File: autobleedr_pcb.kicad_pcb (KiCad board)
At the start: 2 copper layers, 4 parts, among them U1 ESP-32, U2 TMC2209, U3 Buck Converter, U4 DRV8874

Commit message: added header pins
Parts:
- added J1: Barrel_Jack, Connector_BarrelJack:BarrelJack_CUI_PJ-063AH_Horizontal, F.Cu at (149.0, 79.5)
- added J2: Conn_01x13_Pin, Connector_PinHeader_2.54mm:PinHeader_1x13_P2.54mm_Vertical, F.Cu at (99.0, 89.7)
- added J3: Conn_01x14_Pin, Connector_PinHeader_2.54mm:PinHeader_1x14_P2.54mm_Vertical, F.Cu at (134.5, 90.1)
- added J4: Conn_01x08_Socket, Connector_PinHeader_2.54mm:PinHeader_1x08_P2.54mm_Vertical, F.Cu at (186.5, 102.4)
- added J5: Conn_01x05_Pin, Connector_PinHeader_2.54mm:PinHeader_1x05_P2.54mm_Vertical, F.Cu at (167.5, 96.9)
- added J6: Conn_01x05_Pin, Connector_PinHeader_2.54mm:PinHeader_1x05_P2.54mm_Vertical, F.Cu at (142.5, 91.4)
- U1: value ESP-32 -> ~
- U2: value TMC2209 -> ~
- U3: value Buck Converter -> ~
- U4: value DRV8874 -> ~
- moved U2 103.8 mm to (193.5, 106.9), turned to -90 degrees
- moved U4 39.4 mm to (148.8, 91.8)
- moved U1 31.6 mm to (104.5, 90.4)
- moved U3 25.3 mm to (133.0, 80.5), turned to 180 degrees
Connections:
- U1 pad 1: unconnected-(U1-EN-Pad1) -> Net-(J2-Pin_1)
- U1 pad 10: unconnected-(U1-D27-Pad10) -> Net-(J2-Pin_10)
- U1 pad 11: unconnected-(U1-D14-Pad11) -> Net-(J2-Pin_11)
- U1 pad 12: unconnected-(U1-D12-Pad12) -> Net-(J2-Pin_12)
- U1 pad 13: unconnected-(U1-D13-Pad13) -> Net-(J2-Pin_13)
- U1 pad 16: unconnected-(U1-3V3-Pad16) -> Net-(J3-Pin_14)
- U1 pad 18: unconnected-(U1-D15-Pad18) -> Net-(J3-Pin_13)
- U1 pad 19: unconnected-(U1-D2-Pad19) -> Net-(J3-Pin_12)
- U1 pad 2: unconnected-(U1-VP-Pad2) -> Net-(J2-Pin_2)
- U1 pad 20: unconnected-(U1-D4-Pad20) -> Net-(J3-Pin_11)
- U1 pad 21: unconnected-(U1-RX2-Pad21) -> Net-(J3-Pin_10)
- U1 pad 22: unconnected-(U1-TX2-Pad22) -> Net-(J3-Pin_9)
- U1 pad 23: unconnected-(U1-D5-Pad23) -> Net-(J3-Pin_8)
- U1 pad 24: unconnected-(U1-D18-Pad24) -> Net-(J3-Pin_7)
- U1 pad 25: unconnected-(U1-D19-Pad25) -> Net-(J3-Pin_6)
- U1 pad 26: unconnected-(U1-D21-Pad26) -> Net-(J3-Pin_5)
- U1 pad 27: unconnected-(U1-RX0-Pad27) -> Net-(J3-Pin_4)
- U1 pad 28: unconnected-(U1-TX0-Pad28) -> Net-(J3-Pin_3)
- U1 pad 29: unconnected-(U1-D22-Pad29) -> Net-(J3-Pin_2)
- U1 pad 3: unconnected-(U1-VN-Pad3) -> Net-(J2-Pin_3)
- U1 pad 30: unconnected-(U1-D23-Pad30) -> Net-(J3-Pin_1)
- U1 pad 4: unconnected-(U1-D34-Pad4) -> Net-(J2-Pin_4)
- U1 pad 5: unconnected-(U1-D35-Pad5) -> Net-(J2-Pin_5)
- U1 pad 6: unconnected-(U1-D32-Pad6) -> Net-(J2-Pin_6)
- U1 pad 7: unconnected-(U1-D33-Pad7) -> Net-(J2-Pin_7)
- U1 pad 8: unconnected-(U1-D25-Pad8) -> Net-(J2-Pin_8)
- U1 pad 9: unconnected-(U1-D26-Pad9) -> Net-(J2-Pin_9)
- U2 pad 10: unconnected-(U2-EN-Pad10) -> Net-(J4-Pin_8)
- U2 pad 3: unconnected-(U2-DIR-Pad3) -> Net-(J4-Pin_1)
- U2 pad 4: unconnected-(U2-STEP-Pad4) -> Net-(J4-Pin_2)
- U2 pad 5: unconnected-(U2-MS1-Pad5) -> Net-(J4-Pin_3)
- U2 pad 6: unconnected-(U2-MS2-Pad6) -> Net-(J4-Pin_4)
- U2 pad 7: unconnected-(U2-DIAG-Pad7) -> Net-(J4-Pin_5)
- U2 pad 8: unconnected-(U2-INDEX-Pad8) -> Net-(J4-Pin_6)
- U2 pad 9: unconnected-(U2-UART-Pad9) -> Net-(J4-Pin_7)
- U4 pad 1: unconnected-(U4-VM-Pad1) -> Net-(J6-Pin_1)
- U4 pad 10: unconnected-(U4-IMODE-Pad10) -> Net-(J5-Pin_3)
- U4 pad 11: unconnected-(U4-OUT2-Pad11) -> Net-(J5-Pin_2)
- U4 pad 12: unconnected-(U4-OUT1-Pad12) -> Net-(J5-Pin_1)
- U4 pad 3: unconnected-(U4-EN/IN1-Pad3) -> Net-(J6-Pin_2)
- U4 pad 4: unconnected-(U4-PH/IN2-Pad4) -> Net-(J6-Pin_3)
- U4 pad 5: unconnected-(U4-PMODE-Pad5) -> Net-(J6-Pin_4)
- U4 pad 7: unconnected-(U4-VREF-Pad7) -> Net-(J6-Pin_5)
- U4 pad 8: unconnected-(U4-CS-Pad8) -> Net-(J5-Pin_5)
- U4 pad 9: unconnected-(U4-FAULT-Pad9) -> Net-(J5-Pin_4)
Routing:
- added copper zone on B.Cu, net GND

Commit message: finished initial PCB
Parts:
- added J7: Screw_Terminal_01x02, TerminalBlock:TerminalBlock_MaiXu_MX126-5.0-02P_1x02_P5.00mm, F.Cu at (149.0, 91.0)
- added J8: Conn_01x02_Pin, Connector_PinHeader_2.54mm:PinHeader_1x02_P2.54mm_Vertical, F.Cu at (139.5, 89.0)
- added J9: Conn_01x02_Pin, Connector_PinHeader_2.54mm:PinHeader_1x02_P2.54mm_Vertical, F.Cu at (139.5, 84.5)
- U1: value ~ -> ESP32
- U2: value ~ -> TMC2209
- U3: value ~ -> Buck Converter
- U4: value ~ -> DRV8874
- moved J6 69.4 mm to (75.2, 74.3)
- moved U4 68.9 mm to (83.5, 69.8)
- moved J5 68.2 mm to (103.0, 74.8)
- moved Dir 50.6 mm to (136.7, 111.7)
- moved J3 50.2 mm to (119.3, 138.0), turned to -90 degrees
- moved U2 48.8 mm to (145.7, 117.0)
- moved J2 20.7 mm to (119.1, 94.5), turned to -90 degrees
- moved U1 19.3 mm to (119.0, 103.0), turned to -90 degrees
- renumbered J4 to Dir
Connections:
- J2 pad 2: Net-(J2-Pin_2) -> unconnected-(J2-Pin_2-Pad2)
- J2 pad 3: Net-(J2-Pin_3) -> unconnected-(J2-Pin_3-Pad3)
- J6 pad 1: Net-(J6-Pin_1) -> unconnected-(J6-Pin_1-Pad1)
- J6 pad 5: Net-(J6-Pin_5) -> unconnected-(J6-Pin_5-Pad5)
- U1 pad 2: Net-(J2-Pin_2) -> unconnected-(J2-Pin_2-Pad2)
- U1 pad 3: Net-(J2-Pin_3) -> unconnected-(J2-Pin_3-Pad3)
- U4 pad 1: Net-(J6-Pin_1) -> unconnected-(J6-Pin_1-Pad1)
- U4 pad 7: Net-(J6-Pin_5) -> unconnected-(J6-Pin_5-Pad5)
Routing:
- net +3.3V: track 0.00 -> 131.3 mm
- net +12V: track 0.00 -> 70.8 mm
- net Net-(J3-Pin_14): track 0.00 -> 10.8 mm
- net unconnected-(J6-Pin_1-Pad1): track 0.00 -> 10.2 mm
- net Net-(J3-Pin_9): track 0.00 -> 9.71 mm
- net Net-(J3-Pin_7): track 0.00 -> 9.71 mm
- net Net-(J3-Pin_5): track 0.00 -> 9.71 mm
- net Net-(J3-Pin_4): track 0.00 -> 9.71 mm
- net Net-(J3-Pin_3): track 0.00 -> 9.71 mm
- net Net-(J3-Pin_2): track 0.00 -> 9.71 mm
- net Net-(J3-Pin_12): track 0.00 -> 9.71 mm
- net Net-(J3-Pin_11): track 0.00 -> 9.71 mm
- net Net-(J3-Pin_8): track 0.00 -> 9.71 mm
- net Net-(J3-Pin_6): track 0.00 -> 9.71 mm
- net Net-(J3-Pin_13): track 0.00 -> 9.71 mm
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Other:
- board outline added: 91 x 78.5 mm
- board text added: "12V"
- board text added: "3.3V"
- board text added: "AutoBleedr"
- board text added: "Vin"

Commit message: resubmit update 1
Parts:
- added J10: XT60 Connector, Connector_AMASS:AMASS_XT60PW-F_1x02_P7.20mm_Horizontal, F.Cu at (141.8, 93.1)
- U1: value ESP32 -> ~
- U2: value TMC2209 -> ~
- U3: value Buck Converter -> ~
- U4: value DRV8874 -> ~
- moved J4 14.5 mm to (124.0, 118.5)
- moved U2 14.5 mm to (133.0, 123.9)
- moved J7 14.1 mm to (145.0, 104.5)
- moved J8 10.8 mm to (128.7, 90.0)
- moved J9 10.8 mm to (128.7, 85.5)
- moved J1 8.06 mm to (145.0, 72.5), turned to 90 degrees
- moved U1 7.46 mm to (111.6, 102.9)
- moved J2 7.46 mm to (111.7, 94.4)
- moved J3 7.46 mm to (111.8, 137.9)
- renumbered Dir to J4
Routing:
- net +3.3V: track 131.3 -> 48.6 mm
- net +12V: track 70.8 -> 38.7 mm
- net Net-(J4-Pin_4): track 9.10 -> 18.2 mm
- net Net-(J4-Pin_8): track 9.10 -> 0.00 mm
- net Net-(J4-Pin_7): track 9.10 -> 0.00 mm
- net Net-(J4-Pin_5): track 9.10 -> 18.2 mm
- net Net-(J4-Pin_6): track 9.10 -> 0.00 mm
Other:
- board text added: "AutoBleedr Version 1"
- board text removed: "AutoBleedr"

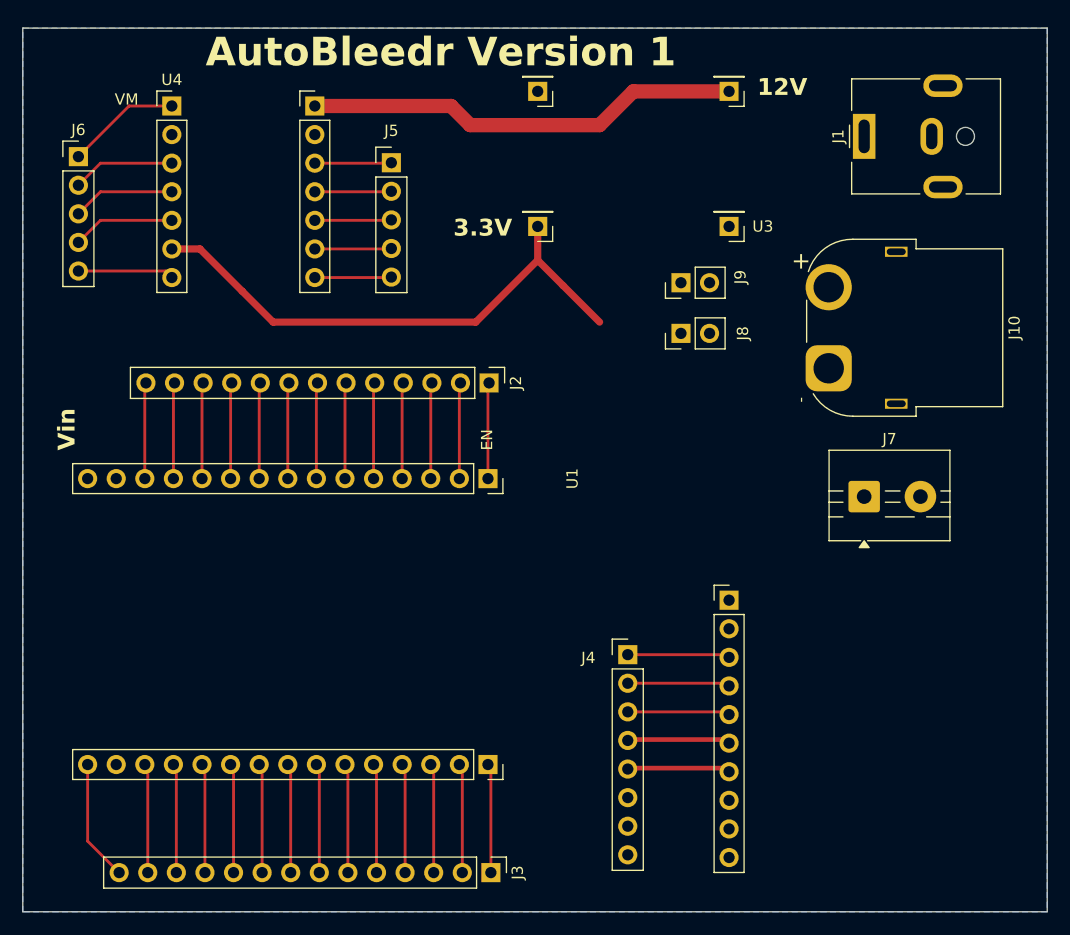
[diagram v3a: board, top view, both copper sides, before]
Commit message: Updated buck converter footprint, added stitching vias, test points, traces
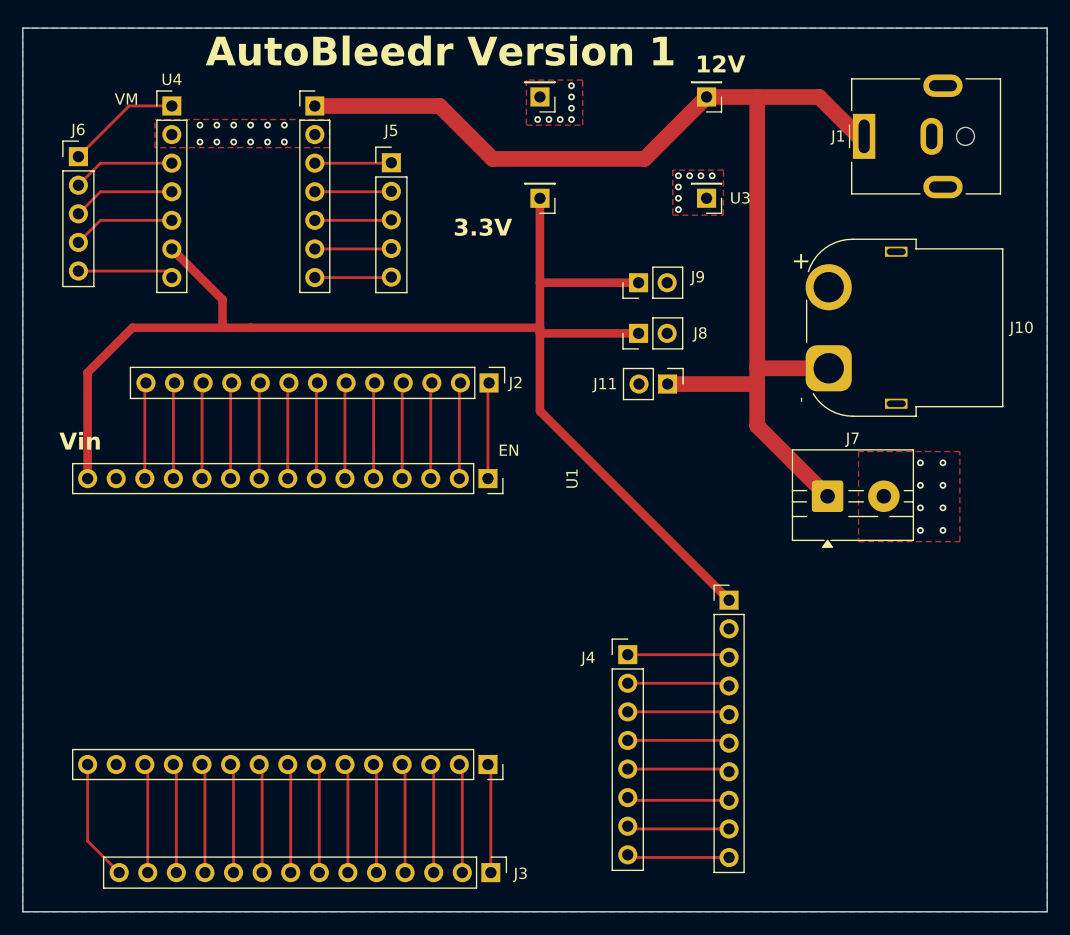
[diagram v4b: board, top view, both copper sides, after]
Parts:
- added J11: Conn_01x02_Pin, Connector_PinHeader_2.54mm:PinHeader_1x02_P2.54mm_Vertical, F.Cu at (127.5, 94.5)
- moved J8 3.77 mm to (125.0, 90.0)
- moved J9 3.77 mm to (125.0, 85.5)
- moved J7 3.25 mm to (141.8, 104.5)
- moved U3 3.20 mm to (131.0, 78.0)
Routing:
- net +3.3V: track 48.6 -> 120.3 mm
- net +12V: track 38.7 -> 106.9 mm
- net Net-(J4-Pin_8): track 0.00 -> 9.10 mm
- net Net-(J4-Pin_7): track 0.00 -> 9.10 mm
- net Net-(J4-Pin_6): track 0.00 -> 9.10 mm
- net Net-(J4-Pin_4): track 18.2 -> 9.44 mm
- net Net-(J4-Pin_5): track 18.2 -> 9.44 mm
- net GND: vias 0 -> 34
- added copper zone on F.Cu, net GND

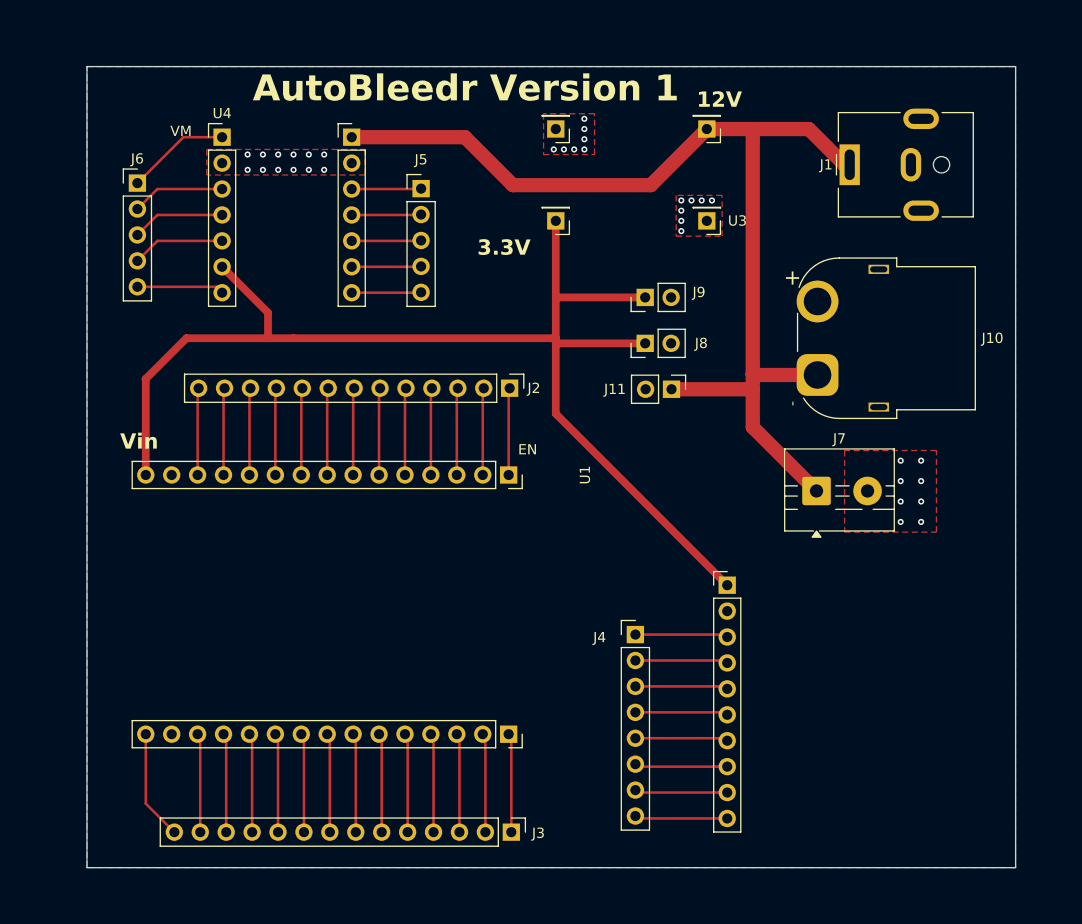
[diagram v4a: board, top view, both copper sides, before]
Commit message: finished labels, screw holes, and trace widths
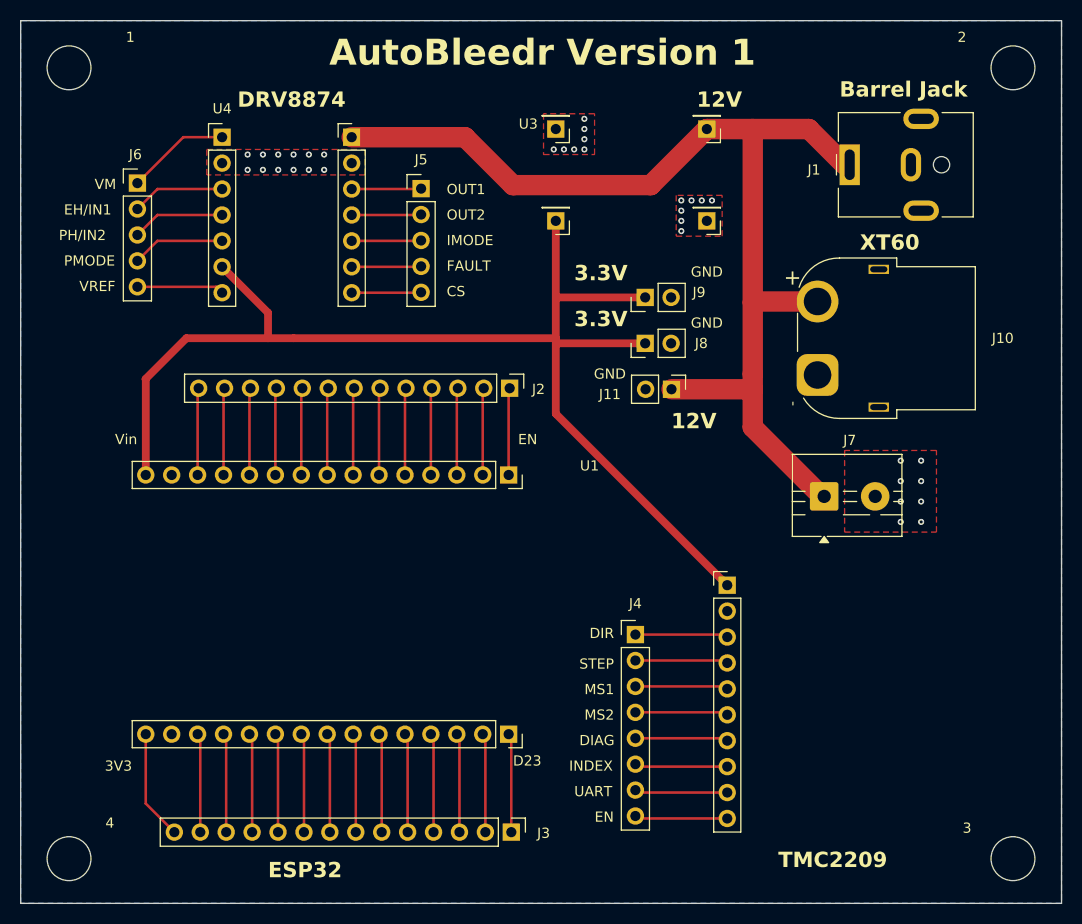
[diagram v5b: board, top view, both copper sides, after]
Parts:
- added 1: MountingHole_4.3mm_M4_ISO7380_Pad, MountingHole:MountingHole_4.3mm_M4_ISO7380_Pad, F.Cu at (68.5, 63.0)
- added 2: MountingHole_4.3mm_M4_ISO7380_Pad, MountingHole:MountingHole_4.3mm_M4_ISO7380_Pad, F.Cu at (161.0, 63.0)
- added 3: MountingHole_4.3mm_M4_ISO7380_Pad, MountingHole:MountingHole_4.3mm_M4_ISO7380_Pad, F.Cu at (161.0, 140.5)
- added 4: MountingHole_4.3mm_M4_ISO7380_Pad, MountingHole:MountingHole_4.3mm_M4_ISO7380_Pad, F.Cu at (68.5, 140.5)
- moved J7 0.92 mm to (142.5, 105.0)
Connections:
- J10 pad 1: +12V -> GND
- J10 pad 2: GND -> +12V
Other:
- board size 91 x 78.5 mm -> 102 x 86.5 mm
- board text added: "3V3"
- board text added: "Barrel Jack"
- board text added: "CS"
- board text added: "D23"
- board text added: "DIAG"
- board text added: "DIR"
- board text added: "DRV8874"
- board text added: "EH/IN1"
- board text added: "EN"
- board text added: "ESP32"
- board text added: "FAULT"
- board text added: "GND"
- board text added: "IMODE"
- board text added: "INDEX"
- board text added: "MS1"
- board text added: "MS2"
- board text added: "OUT1"
- board text added: "OUT2"
- board text added: "PH/IN2"
- board text added: "PMODE"
- board text added: "STEP"
- board text added: "TMC2209"
- board text added: "UART"
- board text added: "VREF"
- board text added: "XT60"
